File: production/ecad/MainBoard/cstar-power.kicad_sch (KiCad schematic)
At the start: 29 parts, among them IC1 LT8648SEV#PBF, U1 AZ1117IH-3.3TRG1

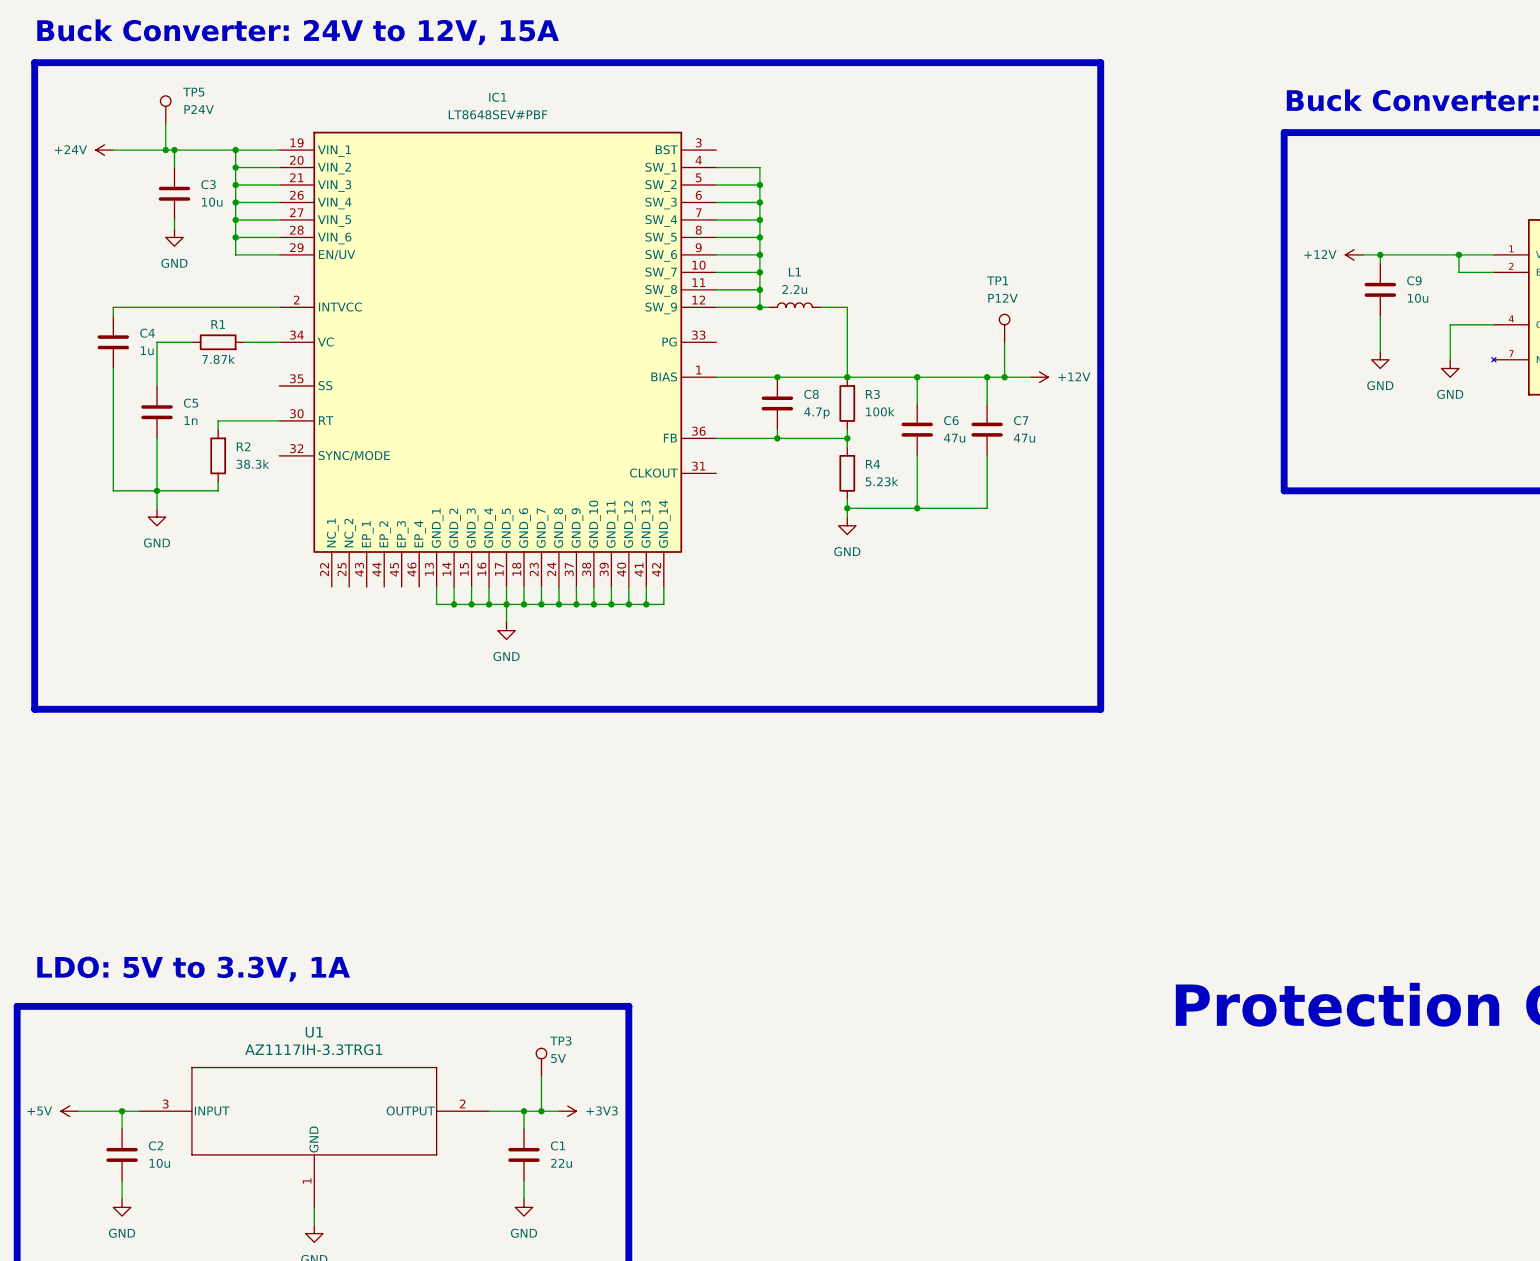
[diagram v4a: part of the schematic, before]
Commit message: 3 fuses added
Circuit Protection Fuses for 12V, 5V, and 3v3 power rails were added.
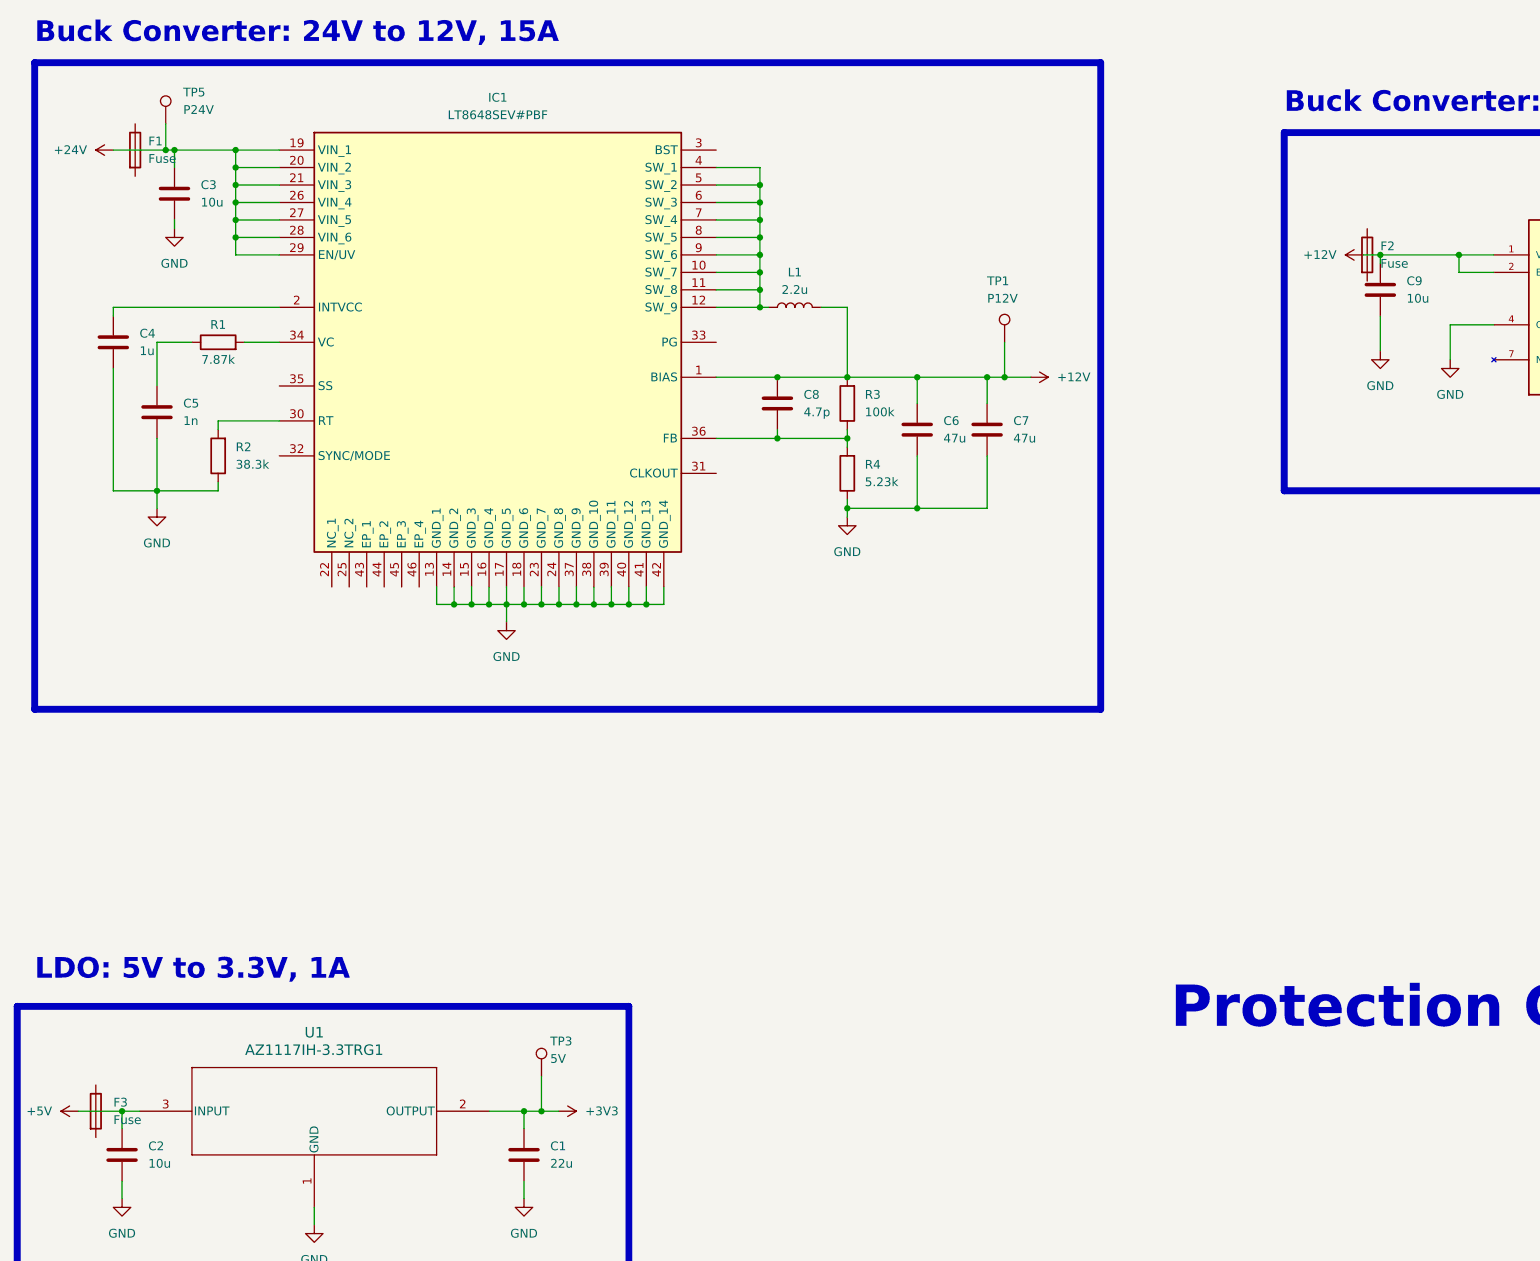
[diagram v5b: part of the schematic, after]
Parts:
- added F1, F2, F3: Fuse, symbol Device:Fuse
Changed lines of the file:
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@@
       (effects (font (size 1.27 1.27)) hide)
     )
-    (pin "2")
-    (pin "1")
+    (pin "1")
+    (pin "2")
     (instances
       (project "cstar-power"
@@
     )
   )
+  (symbol (lib_id "Device:Fuse") (at 234.315 80.01 0) (unit 1)
+    (in_bom yes) (on_board yes) (dnp no) (fields_autoplaced)
+    (property "Reference" "F2" (at 236.22 78.74 0)
+      (effects (font (size 1.27 1.27)) (justify left))
+    )
+    (property "Value" "Fuse" (at 236.22 81.28 0)
+      (effects (font (size 1.27 1.27)) (justify left))
+    )
+    (property "Footprint" "" (at 232.537 80.01 90)
+      (effects (font (size 1.27 1.27)) hide)
+    )
+    (property "Datasheet" "~" (at 234.315 80.01 0)
+      (effects (font (size 1.27 1.27)) hide)
+    )
+    (pin "1")
+    (pin "2")
+    (instances
+      (project "cstar-power"
+        (path "/7edd775e-47a6-46f9-8e16-808bdf3a0e15"
+          (reference "F2") (unit 1)
+        )
+      )
+    )
+  )
   (symbol (lib_id "Device:R") (at 67.31 92.71 90) (unit 1)
     (in_bom yes) (on_board yes) (dnp no)
@@
       (effects (font (size 1.27 1.27)) hide)
     )
-    (pin "2")
-    (pin "1")
+    (pin "1")
+    (pin "2")
     (instances
       (project "cstar-power"
@@
       (effects (font (size 1.27 1.27)) hide)
     )
-    (pin "2")
-    (pin "1")
+    (pin "1")
+    (pin "2")
     (instances
       (project "cstar-power"
@@
       (effects (font (size 1.27 1.27) italic) hide)
     )
+    (pin "2")
+    (pin "1")
     (pin "3")
-    (pin "1")
-    (pin "2")
     (instances
       (project "cstar-power"
@@
       (effects (font (size 1.27 1.27)) (justify left top) hide)
     )
-    (pin "28")
-    (pin "41")
-    (pin "45")
-    (pin "8")
-    (pin "1")
+    (pin "1")
+    (pin "10")
+    (pin "11")
     (pin "12")
     (pin "13")
+    (pin "14")
+    (pin "15")
     (pin "16")
-    (pin "2")
+    (pin "17")
+    (pin "18")
+    (pin "19")
+    (pin "2")
+    (pin "20")
+    (pin "21")
+    (pin "22")
+    (pin "23")
+    (pin "24")
+    (pin "25")
+    (pin "26")
+    (pin "27")
+    (pin "28")
     (pin "29")
+    (pin "3")
+    (pin "30")
+    (pin "31")
     (pin "32")
+    (pin "33")
+    (pin "34")
     (pin "35")
-    (pin "19")
+    (pin "36")
+    (pin "37")
+    (pin "38")
     (pin "39")
     (pin "4")
-    (pin "37")
-    (pin "22")
-    (pin "26")
-    (pin "23")
-    (pin "33")
-    (pin "21")
+    (pin "40")
+    (pin "41")
     (pin "42")
-    (pin "38")
     (pin "43")
     (pin "44")
-    (pin "24")
-    (pin "11")
-    (pin "31")
+    (pin "45")
     (pin "46")
+    (pin "5")
+    (pin "6")
     (pin "7")
-    (pin "34")
-    (pin "20")
-    (pin "18")
-    (pin "27")
-    (pin "3")
-    (pin "6")
-    (pin "10")
-    (pin "30")
+    (pin "8")
     (pin "9")
-    (pin "17")
-    (pin "14")
-    (pin "25")
-    (pin "15")
-    (pin "40")
-    (pin "5")
-    (pin "36")
     (instances
       (project "cstar-power"
@@
     )
   )
+  (symbol (lib_id "Device:Fuse") (at 55.245 64.77 0) (unit 1)
+    (in_bom yes) (on_board yes) (dnp no) (fields_autoplaced)
+    (property "Reference" "F1" (at 57.15 63.5 0)
+      (effects (font (size 1.27 1.27)) (justify left))
+    )
+    (property "Value" "Fuse" (at 57.15 66.04 0)
+      (effects (font (size 1.27 1.27)) (justify left))
+    )
+    (property "Footprint" "" (at 53.467 64.77 90)
+      (effects (font (size 1.27 1.27)) hide)
+    )
+    (property "Datasheet" "~" (at 55.245 64.77 0)
+      (effects (font (size 1.27 1.27)) hide)
+    )
+    (pin "1")
+    (pin "2")
+    (instances
+      (project "cstar-power"
+        (path "/7edd775e-47a6-46f9-8e16-808bdf3a0e15"
+          (reference "F1") (unit 1)
+        )
+      )
+    )
+  )
   (symbol (lib_id "power:GND") (at 81.28 220.98 0) (unit 1)
     (in_bom yes) (on_board yes) (dnp no) (fields_autoplaced)
@@
       (effects (font (size 1.27 1.27)) (justify bottom) hide)
     )
+    (pin "1")
     (pin "2")
     (pin "3")
-    (pin "6")
     (pin "4")
     (pin "5")
-    (pin "1")
+    (pin "6")
+    (pin "7")
+    (pin "8")
     (pin "9")
-    (pin "8")
-    (pin "7")
     (instances
       (project "cstar-power"
@@
       (effects (font (size 1.27 1.27)) hide)
     )
-    (pin "2")
-    (pin "1")
+    (pin "1")
+    (pin "2")
     (instances
       (project "cstar-power"
@@
         )
       )
+    )
+  )
+  (symbol (lib_id "Device:Fuse") (at 49.53 204.47 0) (unit 1)
+    (in_bom yes) (on_board yes) (dnp no) (fields_autoplaced)
+    (property "Reference" "F3" (at 52.07 203.2 0)
+      (effects (font (size 1.27 1.27)) (justify left))
+    )
+    (property "Value" "Fuse" (at 52.07 205.74 0)
+      (effects (font (size 1.27 1.27)) (justify left))
+    )
+    (property "Footprint" "" (at 47.752 204.47 90)
+      (effects (font (size 1.27 1.27)) hide)
+    )
+    (property "Datasheet" "~" (at 49.53 204.47 0)
+      (effects (font (size 1.27 1.27)) hide)
+    )
+    (pin "1")
+    (pin "2")
+    (instances
+      (project "cstar-power"
+        (path "/7edd775e-47a6-46f9-8e16-808bdf3a0e15"
+          (reference "F3") (unit 1)
+        )
+      )

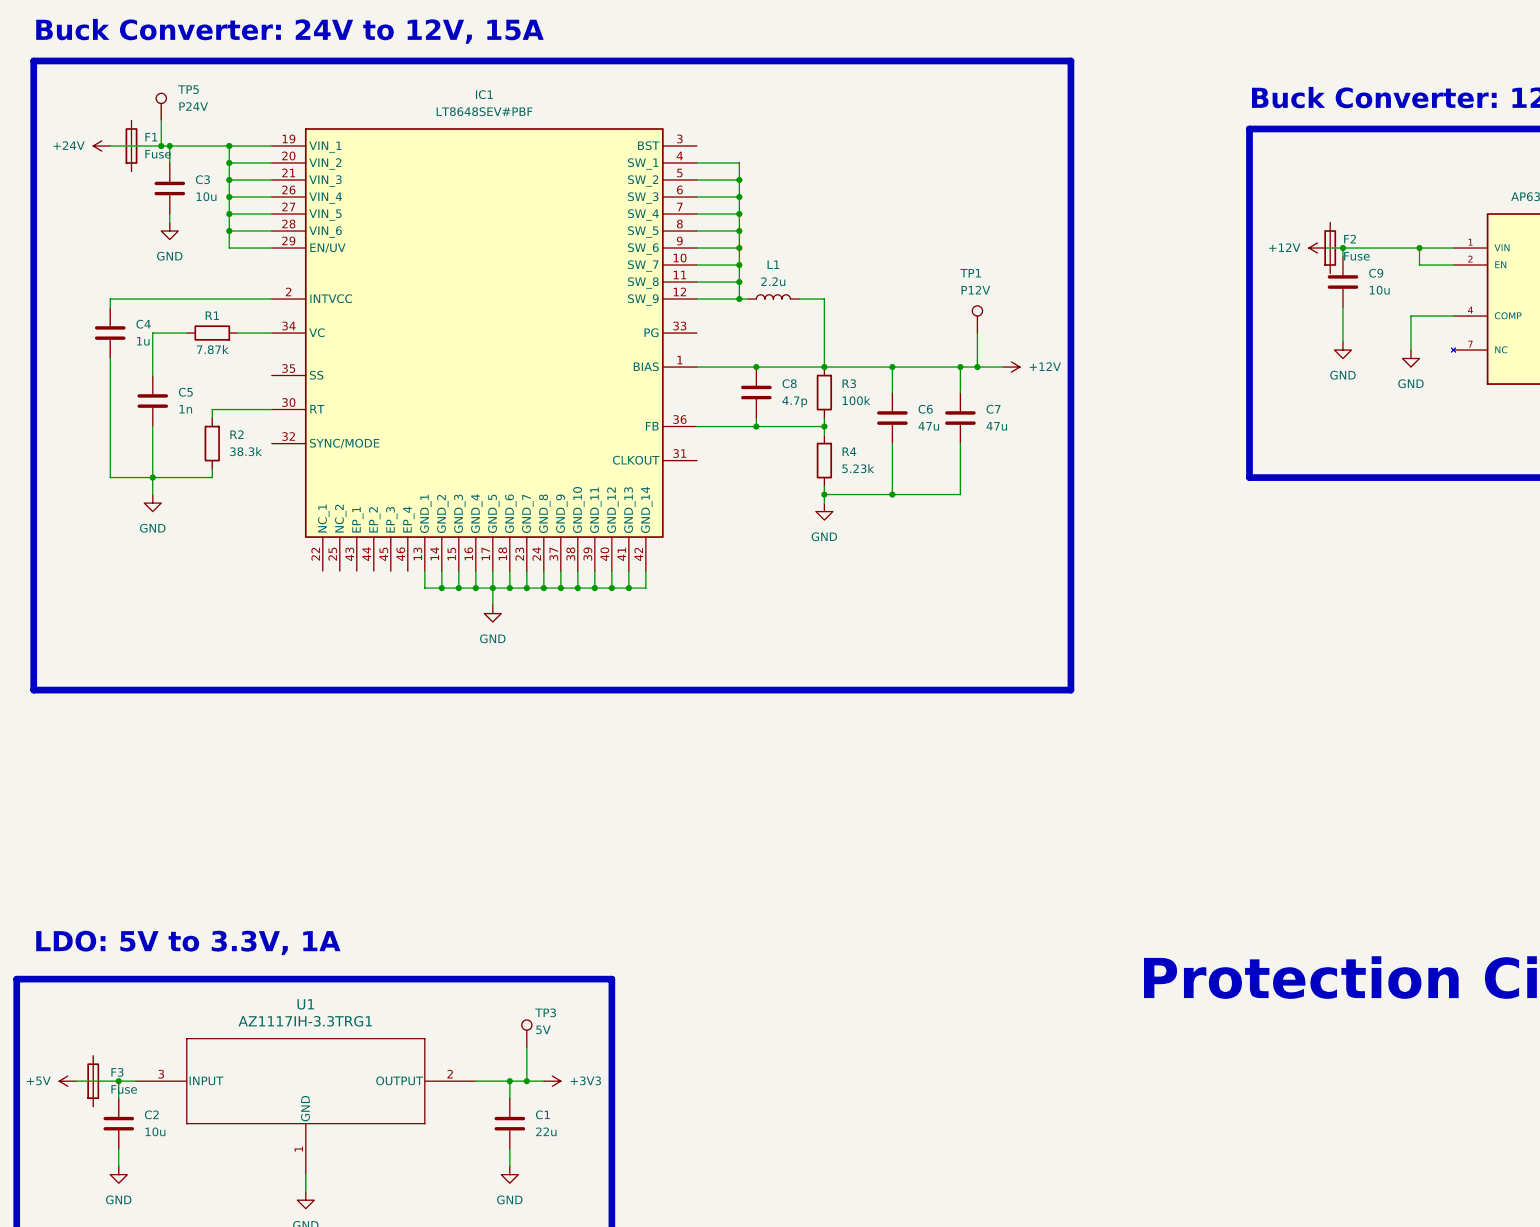
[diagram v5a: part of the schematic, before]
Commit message: Edited fuse values
Changed fuse values to 5A in symbol properties.
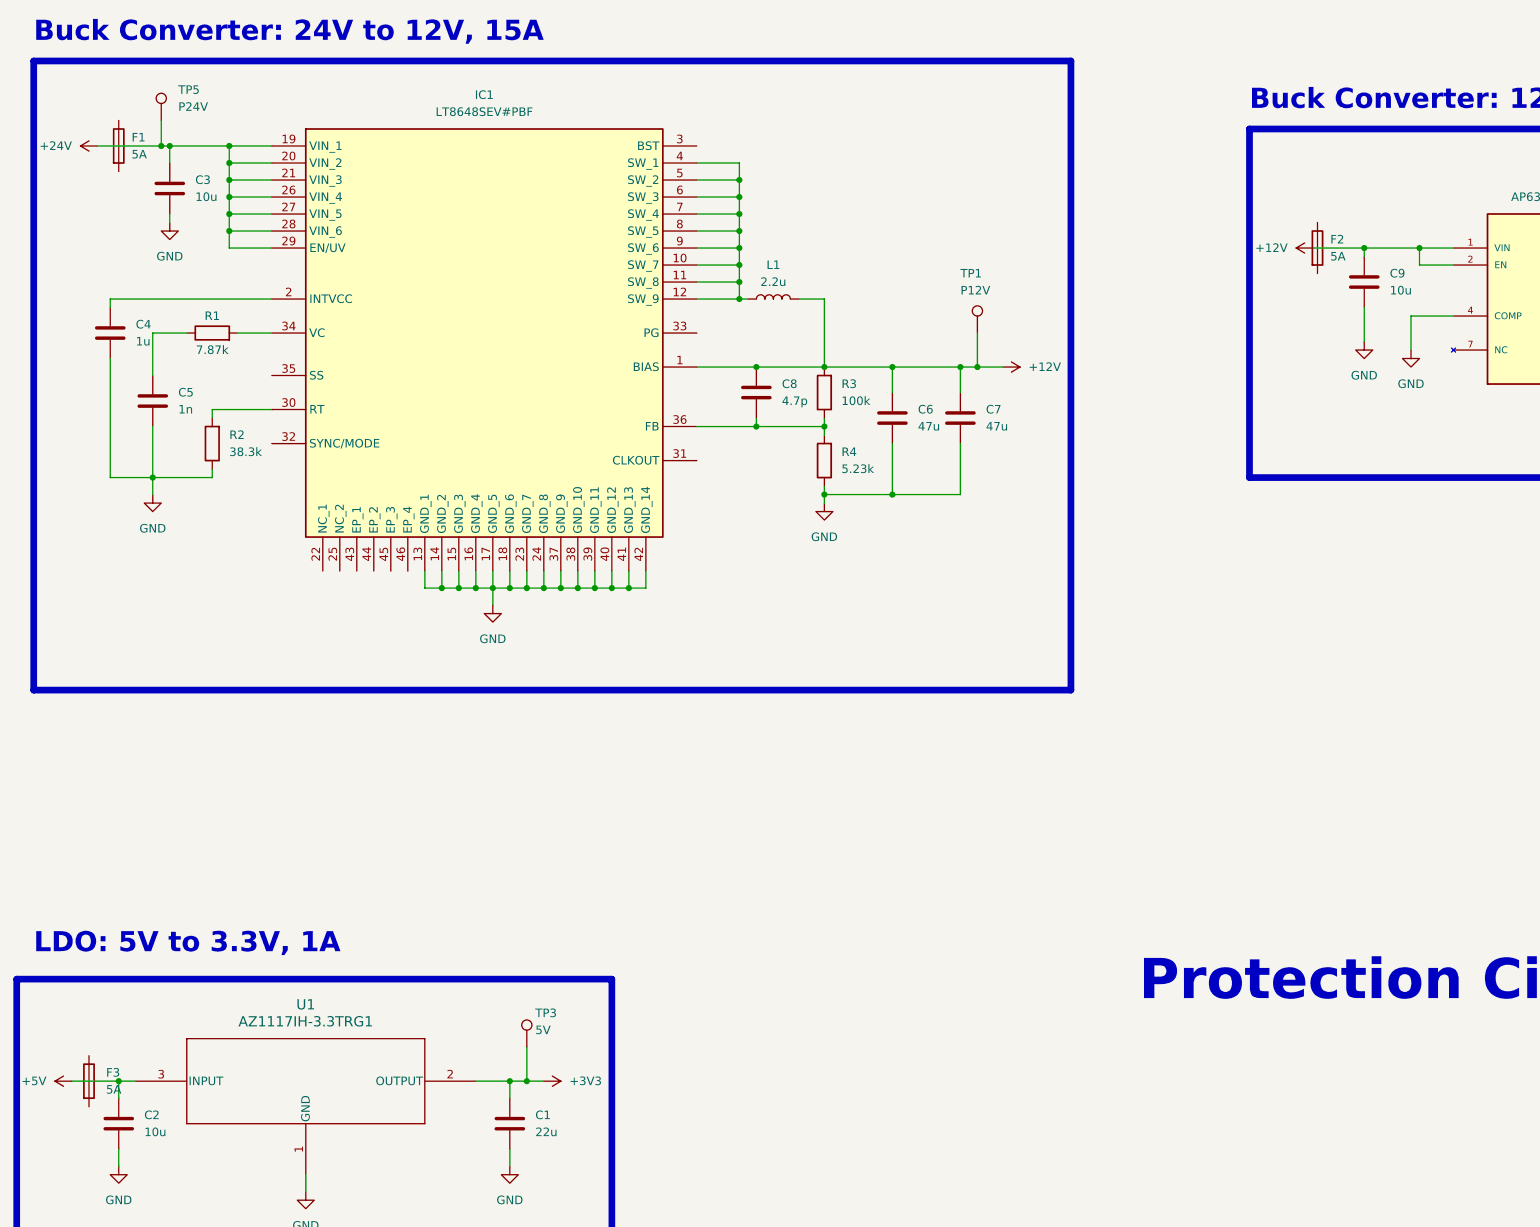
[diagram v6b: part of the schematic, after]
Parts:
- F1, F2, F3: value Fuse -> 5A
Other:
- moved on the sheet: C9, F1, F2, F3

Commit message: Edited description text
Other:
- note added: "Protection Circutry: Three 5A Circuit Protection Fuses were added to the 12V, 5V, and 3v3 power rails."
- note removed: "Protection Circutry to be added"
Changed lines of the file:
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@@
     (effects (font (size 6 6) bold) (justify left bottom))
   )
-  (text "Protection Circutry to be added" (at 205.74 193.04 0)
+  (text "Protection Circutry:  Three 5A Circuit Protection Fuses were added to the 12V, 5V, and 3v3 power rails."
+    (at 17.78 254 0)
     (effects (font (size 6 6) bold (color 255 2 31 1)) (justify left bottom))
   )
